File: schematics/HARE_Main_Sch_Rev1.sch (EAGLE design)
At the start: 96 parts, among them IC1 NE5532N, IC2 NE5532N, IC3 FT232RL, IC4 NE5532N, IC5 7805DT, IC6 AT25P, J1 9V, J2 STEREOSW, J3 STEREOSW, Q1 16 MHz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

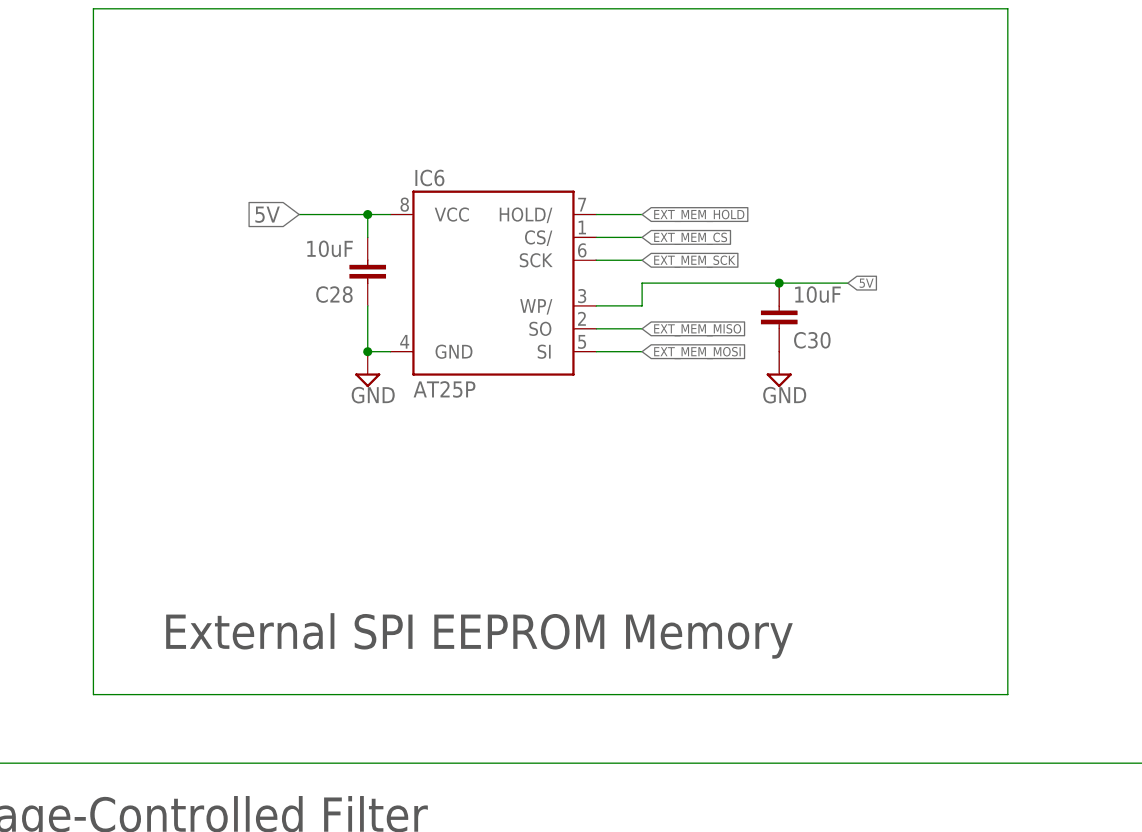
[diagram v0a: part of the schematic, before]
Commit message: Switch memory chip to SRAM
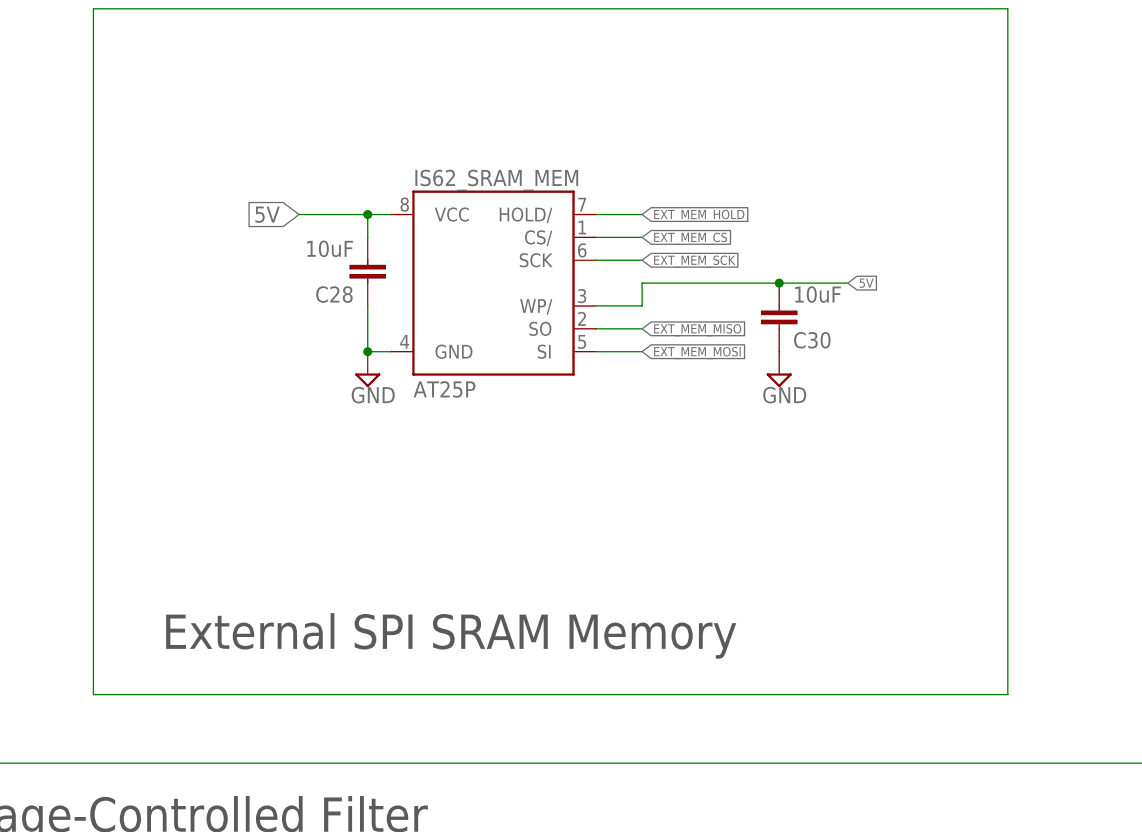
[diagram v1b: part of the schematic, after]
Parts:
- renumbered IC6 to IS62_SRAM_MEM
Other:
- note added: "External SPI SRAM Memory"
- note removed: "External SPI EEPROM Memory"
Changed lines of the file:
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@@
 <part name="R38" library="resistor" deviceset="R-US_" device="R0805" value="1k"/>
 <part name="SUPPLY37" library="supply2" deviceset="GND" device=""/>
-<part name="IC6" library="atmel" library_urn="urn:adsk.eagle:library:105" deviceset="AT25*" device="P" package3d_urn="urn:adsk.eagle:package:4324/1"/>
+<part name="IS62_SRAM_MEM" library="atmel" library_urn="urn:adsk.eagle:library:105" deviceset="AT25*" device="P" package3d_urn="urn:adsk.eagle:package:4324/1"/>
 <part name="SUPPLY38" library="supply2" deviceset="GND" device=""/>
 <part name="C28" library="resistor" deviceset="C-EU" device="C0805K" value="10uF"/>
@@
 <text x="27.94" y="119.38" size="3.81" layer="97" font="vector" ratio="12">Analog Input Circuitry</text>
 <text x="187.96" y="119.38" size="3.81" layer="97" font="vector" ratio="12">PWMDAC Filter</text>
-<text x="441.96" y="139.7" size="3.81" layer="97" font="vector" ratio="12">External SPI EEPROM Memory</text>
+<text x="441.96" y="139.7" size="3.81" layer="97" font="vector" ratio="12">External SPI SRAM Memory</text>
 </plain>
 <instances>
@@
 <instance part="R38" gate="G$1" x="170.18" y="198.12" rot="R90"/>
 <instance part="SUPPLY37" gate="GND" x="170.18" y="187.96"/>
-<instance part="IC6" gate="G$1" x="477.52" y="180.34"/>
+<instance part="IS62_SRAM_MEM" gate="G$1" x="477.52" y="180.34"/>
 <instance part="SUPPLY38" gate="GND" x="464.82" y="170.18"/>
 <instance part="C28" gate="G$1" x="464.82" y="180.34" rot="R180"/>
@@
 </segment>
 <segment>
-<pinref part="IC6" gate="G$1" pin="GND"/>
+<pinref part="IS62_SRAM_MEM" gate="G$1" pin="GND"/>
 <wire x1="467.36" y1="172.72" x2="464.82" y2="172.72" width="0.1524" layer="91"/>
 <pinref part="SUPPLY38" gate="GND" pin="GND"/>
@@
 </segment>
 <segment>
-<pinref part="IC6" gate="G$1" pin="VCC"/>
+<pinref part="IS62_SRAM_MEM" gate="G$1" pin="VCC"/>
 <pinref part="C28" gate="G$1" pin="2"/>
 <label x="457.2" y="187.96" size="1.778" layer="95" rot="R180" xref="yes"/>
@@
 <pinref part="C30" gate="G$1" pin="2"/>
 <wire x1="510.54" y1="180.34" x2="518.16" y2="180.34" width="0.1524" layer="91"/>
-<pinref part="IC6" gate="G$1" pin="WP/"/>
+<pinref part="IS62_SRAM_MEM" gate="G$1" pin="WP/"/>
 <wire x1="510.54" y1="180.34" x2="495.3" y2="180.34" width="0.1524" layer="91"/>
 <wire x1="495.3" y1="180.34" x2="495.3" y2="177.8" width="0.1524" layer="91"/>
@@
 </segment>
 <segment>
-<pinref part="IC6" gate="G$1" pin="SCK"/>
+<pinref part="IS62_SRAM_MEM" gate="G$1" pin="SCK"/>
 <wire x1="490.22" y1="182.88" x2="495.3" y2="182.88" width="0.1524" layer="91"/>
 <label x="495.3" y="182.88" size="1.016" layer="95" xref="yes"/>
@@
 </segment>
 <segment>
-<pinref part="IC6" gate="G$1" pin="SO"/>
+<pinref part="IS62_SRAM_MEM" gate="G$1" pin="SO"/>
 <wire x1="490.22" y1="175.26" x2="495.3" y2="175.26" width="0.1524" layer="91"/>
 <label x="495.3" y="175.26" size="1.016" layer="95" xref="yes"/>
@@
 </segment>
 <segment>
-<pinref part="IC6" gate="G$1" pin="SI"/>
+<pinref part="IS62_SRAM_MEM" gate="G$1" pin="SI"/>
 <wire x1="490.22" y1="172.72" x2="495.3" y2="172.72" width="0.1524" layer="91"/>
 <label x="495.3" y="172.72" size="1.016" layer="95" xref="yes"/>
@@
 </segment>
 <segment>
-<pinref part="IC6" gate="G$1" pin="CS/"/>
+<pinref part="IS62_SRAM_MEM" gate="G$1" pin="CS/"/>
 <wire x1="490.22" y1="185.42" x2="495.3" y2="185.42" width="0.1524" layer="91"/>
 <label x="495.3" y="185.42" size="1.016" layer="95" xref="yes"/>
@@
 </segment>
 <segment>
-<pinref part="IC6" gate="G$1" pin="HOLD/"/>
+<pinref part="IS62_SRAM_MEM" gate="G$1" pin="HOLD/"/>
 <wire x1="490.22" y1="187.96" x2="495.3" y2="187.96" width="0.1524" layer="91"/>
 <label x="495.3" y="187.96" size="1.016" layer="95" rot="MR180" xref="yes"/>

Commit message: fix WP pin on SRAM chip to DNU
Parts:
- removed C30: 10uF, resistor:C-EUC0805K
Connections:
- net 5V: no longer C30.2, IS62_SRAM_MEM.WP/
- net GND: now also IS62_SRAM_MEM.WP/; no longer C30.1
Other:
- note added: "DNU"
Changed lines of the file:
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@@
 <part name="C28" library="resistor" deviceset="C-EU" device="C0805K" value="10uF"/>
 <part name="SUPPLY41" library="supply2" deviceset="GND" device=""/>
-<part name="C30" library="resistor" deviceset="C-EU" device="C0805K" value="10uF"/>
 </parts>
 <sheets>
@@
 <text x="187.96" y="119.38" size="3.81" layer="97" font="vector" ratio="12">PWMDAC Filter</text>
 <text x="441.96" y="139.7" size="3.81" layer="97" font="vector" ratio="12">External SPI SRAM Memory</text>
+<text x="482.6" y="177.8" size="1.778" layer="93">DNU</text>
+<text x="490.22" y="177.8" size="1.778" layer="91">DNU</text>
 </plain>
 <instances>
@@
 <instance part="SUPPLY38" gate="GND" x="464.82" y="170.18"/>
 <instance part="C28" gate="G$1" x="464.82" y="180.34" rot="R180"/>
-<instance part="SUPPLY41" gate="GND" x="510.54" y="170.18"/>
-<instance part="C30" gate="G$1" x="510.54" y="175.26" rot="MR180"/>
+<instance part="SUPPLY41" gate="GND" x="510.54" y="175.26"/>
 </instances>
 <busses>
@@
 </segment>
 <segment>
-<pinref part="C30" gate="G$1" pin="1"/>
+<pinref part="IS62_SRAM_MEM" gate="G$1" pin="WP/"/>
 <pinref part="SUPPLY41" gate="GND" pin="GND"/>
+<wire x1="490.22" y1="177.8" x2="510.54" y2="177.8" width="0.1524" layer="91"/>
 </segment>
 </net>
@@
 <junction x="464.82" y="187.96"/>
 </segment>
-<segment>
-<label x="518.16" y="180.34" size="1.016" layer="95" xref="yes"/>
-<pinref part="C30" gate="G$1" pin="2"/>
-<wire x1="510.54" y1="180.34" x2="518.16" y2="180.34" width="0.1524" layer="91"/>
-<pinref part="IS62_SRAM_MEM" gate="G$1" pin="WP/"/>
-<wire x1="510.54" y1="180.34" x2="495.3" y2="180.34" width="0.1524" layer="91"/>
-<wire x1="495.3" y1="180.34" x2="495.3" y2="177.8" width="0.1524" layer="91"/>
-<wire x1="495.3" y1="177.8" x2="490.22" y2="177.8" width="0.1524" layer="91"/>
-<junction x="510.54" y="180.34"/>
-</segment>
-</net>
+</net>
